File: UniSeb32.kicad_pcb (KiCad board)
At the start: 4 copper layers, 72 x 100 mm, 60 parts, among them J1 IO, J101 Micro_SD_Card_Det, J2 ARJM11C7-114-BA-EW2, J3 Conn_02x05_Odd_Even, J6 SDS011, J7 Conn_01x02_Female, J8 Conn_01x02_Female, U1 mini_esp32, U2 LAN8720A, U3 AMS1117-3.3, U4 AMS5915, U5 module_bme280, U6 RT9400, U7 MCP23008-xSS, U8 HLK-PM01, X1 233-508, X2 233-503, X3 233-504

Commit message: .
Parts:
- removed C5, C6, C7, C8: 10p, Capacitor_SMD:C_0603_1608Metric
- added D101: ESD3.3V88D-LA, Diode_SMD:D_SOD-923, B.Cu at (167.1, 66.9)
- added D102: ESD3.3V88D-LA, Diode_SMD:D_SOD-923, B.Cu at (165.0, 67.1)
- added D103: ESD3.3V88D-LA, Diode_SMD:D_SOD-923, B.Cu at (161.7, 67.1)
- added D104: ESD3.3V88D-LA, Diode_SMD:D_SOD-923, B.Cu at (159.3, 67.1)
- added R101: 10k, Resistor_SMD:R_0603_1608Metric, B.Cu at (159.5, 58.7)
- C3: value 22µ -> 22u
- L1: value L -> FB0805/600R/2A
- moved R12 0.61 mm to (159.9, 62.0), turned to 0 degrees
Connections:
- J2 pad 11: 3V3-2 -> Net-(J2-RLED+)
- J2 pad 12: Net-(J2-Pad12) -> Net-(J2-RLED-)
- R12 pad 1: Net-(J2-Pad12) -> Net-(J2-RLED+)
- R12 pad 2: GND -> 3V3-2
- U2 pad 2: unconnected-(U2-Pad2) -> Net-(J2-RLED-)
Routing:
- net Net-(J2-RLED-): track 0.00 -> 66.1 mm, vias 0 -> 2
- net Net-(J2-Pad12): track 6.44 -> 0.00 mm
- net Net-(J2-RLED+): track 0.00 -> 3.95 mm
- net GND: track 0.00 -> 3.39 mm
- net /TX_P: track 59.7 -> 60.7 mm
- net /RX_N: track 46.5 -> 47.3 mm
- net /RX_P: track 45.4 -> 46.2 mm
- net /TX_N: track 60.1 -> 60.8 mm
- net 3V3-2: track 80.8 -> 81.0 mm, vias 9 -> 10

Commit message: .
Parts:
- removed JP3: SolderJumper_2_Open, Jumper:SolderJumper-2_P1.3mm_Open_Pad1.0x1.5mm
- added C5: 100n, Capacitor_SMD:C_0603_1608Metric, B.Cu at (158.8, 90.5)
- C14, C15: footprint Capacitor_SMD:C_0603_1608Metric -> Capacitor_SMD:C_1206_3216Metric
- moved C15 2.55 mm to (171.5, 61.8)
- moved C14 2.51 mm to (152.8, 61.8)
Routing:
- net /SCL: track 121.3 -> 123.6 mm
- net Net-(C15-Pad1): track 2.62 -> 4.62 mm
- net Net-(C14-Pad1): track 2.62 -> 4.52 mm
- net 3V3-2: track 81.0 -> 82.7 mm
- net /SDA: track 117.4 -> 118.1 mm
- net +5V: track 234.8 -> 235.4 mm

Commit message: finished routing
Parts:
- removed C11: 10n, Capacitor_SMD:C_0603_1608Metric
- removed C14, C15: 1n, Capacitor_SMD:C_1206_3216Metric
- removed C3: 22u, Capacitor_SMD:C_1206_3216Metric
- removed C9: 10u, Capacitor_SMD:C_0603_1608Metric
- removed D102, D103, D104: ESD3.3V88D-LA, Diode_SMD:D_SOD-923
- removed R14: 12.1k, Resistor_SMD:R_0603_1608Metric
- removed R16, R19, R20: 10k, Resistor_SMD:R_0603_1608Metric
- removed U2: LAN8720A, Package_DFN_QFN:QFN-24-1EP_4x4mm_P0.5mm_EP2.6x2.6mm
- added C101: 100n, Capacitor_SMD:C_0603_1608Metric, B.Cu at (165.8, 91.0)
- added C102: 47µ, Capacitor_SMD:C_0805_2012Metric, B.Cu at (148.2, 107.8)
- added C103: 47µ, Capacitor_SMD:C_0805_2012Metric, B.Cu at (151.0, 107.8)
- added C104: 100n, Capacitor_SMD:C_0603_1608Metric, B.Cu at (162.0, 105.5)
- added C16: 100n, Capacitor_SMD:C_0603_1608Metric, B.Cu at (157.5, 91.0)
- added R102: 10k, Resistor_SMD:R_0603_1608Metric, B.Cu at (166.0, 58.8)
- added U101: RTL8201F-VB-CG, UniSeb32:QFN_8201F-VB-CG_RTK, B.Cu at (163.8, 98.0)
- C12: value 2.2µ -> 47µ; footprint Capacitor_SMD:C_0603_1608Metric -> Capacitor_SMD:C_0805_2012Metric
- D101: value ESD3.3V88D-LA -> SM712_SOT23; footprint Diode_SMD:D_SOD-923 -> Package_TO_SOT_SMD:SOT-23
- R15: value 10k -> 2.49k 1%
- moved D101 43.2 mm to (154.5, 108.2), turned to -90 degrees
- moved C5 23.7 mm to (173.5, 72.0), turned to 180 degrees
- moved C4 21.4 mm to (159.8, 91.0), turned to -90 degrees
- moved C12 15.6 mm to (158.5, 106.5)
- moved R18 14.9 mm to (161.8, 91.0), turned to 90 degrees
- moved C13 14.2 mm to (158.2, 102.8), turned to -90 degrees
- moved R15 11.8 mm to (160.2, 102.8), turned to 90 degrees
- moved C10 4.67 mm to (164.8, 103.8)
- moved R17 4.27 mm to (169.8, 100.0)
- moved R10 3.25 mm to (155.5, 98.0), turned to -90 degrees
- moved R11 3.25 mm to (157.5, 97.5), turned to 90 degrees
- moved R13 3.25 mm to (157.5, 94.2), turned to -90 degrees
- moved R9 3.25 mm to (155.5, 101.2), turned to 90 degrees
- moved L1 1.00 mm to (153.5, 104.8), turned to 0 degrees
- moved R8 0.67 mm to (164.5, 62.0), turned to 180 degrees
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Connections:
- C10 pad 1: 3V3-2 -> Net-(U101-DVDD10OUT)
- C12 pad 1: Net-(U2-VDDCR) -> +3.3VA
- C13 pad 1: +3.3V -> Net-(U101-AVDD10OUT)
- C4 pad 2: 3V3-2 -> +3.3VA
- C5 pad 2: 3V3-2 -> Net-(J2-RCT)
- D101 pad 1: /TX_P -> +3.3V
- D101 pad 2: GND -> +3.3VA
- J2 pad 12: Net-(J2-RLED-) -> GND
- J2 pad 14: Net-(J2-LLED-) -> GND
- J2 pad 4: 3V3-2 -> Net-(J2-RCT)
- J2 pad 9: 3V3-2 -> Net-(J2-RCT)
- J2 pad SH1: Net-(C15-Pad1) -> GND
- J2 pad SH2: Net-(C14-Pad1) -> GND
- L1 pad 2: 3V3-2 -> +3.3VA
- R10 pad 1: 3V3-2 -> Net-(C16-Pad1)
- R101 pad 2: Net-(J2-RLED-) -> Net-(U101-LED1/PHYAD[1])
- R11 pad 1: 3V3-2 -> Net-(C16-Pad1)
- R12 pad 1: Net-(J2-RLED+) -> Net-(U101-LED1/PHYAD[1])
- R12 pad 2: 3V3-2 -> Net-(J2-RLED+)
- R13 pad 1: 3V3-2 -> Net-(C16-Pad1)
- R17 pad 2: 3V3-2 -> +3.3V
- R18 pad 1: /EMAC_CRS_DV -> Net-(U101-RXDV)
- R18 pad 2: 3V3-2 -> +3.3V
- R8 pad 1: Net-(J2-LLED-) -> Net-(J2-LLED+)
- R8 pad 2: GND -> Net-(U101-LED0/PHYAD[0]/PMEB)
- R9 pad 1: 3V3-2 -> Net-(C16-Pad1)
- U1 pad 2: unconnected-(U1-RST-Pad2) -> /RST
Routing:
- net 3V3-2: track 82.7 -> 0.00 mm, vias 10 -> 0
- net Net-(U101-LED1/PHYAD[1]): track 0.00 -> 71.9 mm, vias 0 -> 4
- net Net-(J2-RLED-): track 65.9 -> 0.00 mm, vias 2 -> 0
- net Net-(U101-LED0/PHYAD[0]/PMEB): track 0.00 -> 61.9 mm, vias 0 -> 2
- net +3.3VA: track 0.00 -> 41.4 mm, vias 0 -> 2
- net Net-(J2-LLED+): track 44.7 -> 3.57 mm, vias 1 -> 0
- net /RST: track 0.00 -> 27.3 mm, vias 0 -> 1
- net Net-(J2-RCT): track 0.00 -> 19.1 mm, vias 0 -> 1
- net Net-(C16-Pad1): track 0.00 -> 18.0 mm, vias 0 -> 3
- net /IO5_RST: track 17.8 -> 0.00 mm
- net /IO17_RCLK: track 11.4 -> 26.8 mm, vias 0 -> 1
- net +3.3V: track 188.8 -> 176.4 mm, vias 6 -> 9
- net GND: track 3.39 -> 10.7 mm, vias 20 -> 26
- net /EMAC_RXD1: track 28.2 -> 20.8 mm
- net /RX_N: track 47.3 -> 40.0 mm
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- added copper zone on In2.Cu, net +3.3V
- removed copper zone on In2.Cu, net 3V3-2

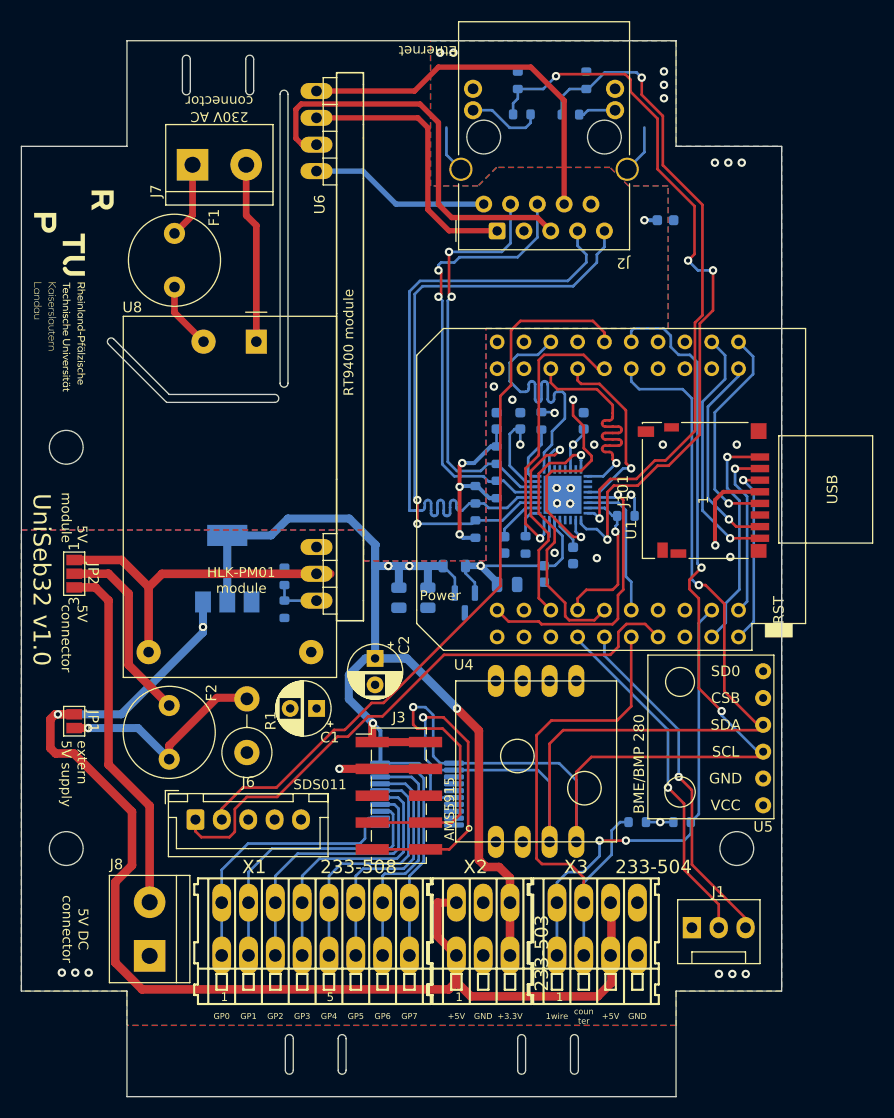
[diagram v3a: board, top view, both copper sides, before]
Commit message: removed SJ1, rename SJ2 -> SJ1, added SJ2 to change pin2 usage of J1
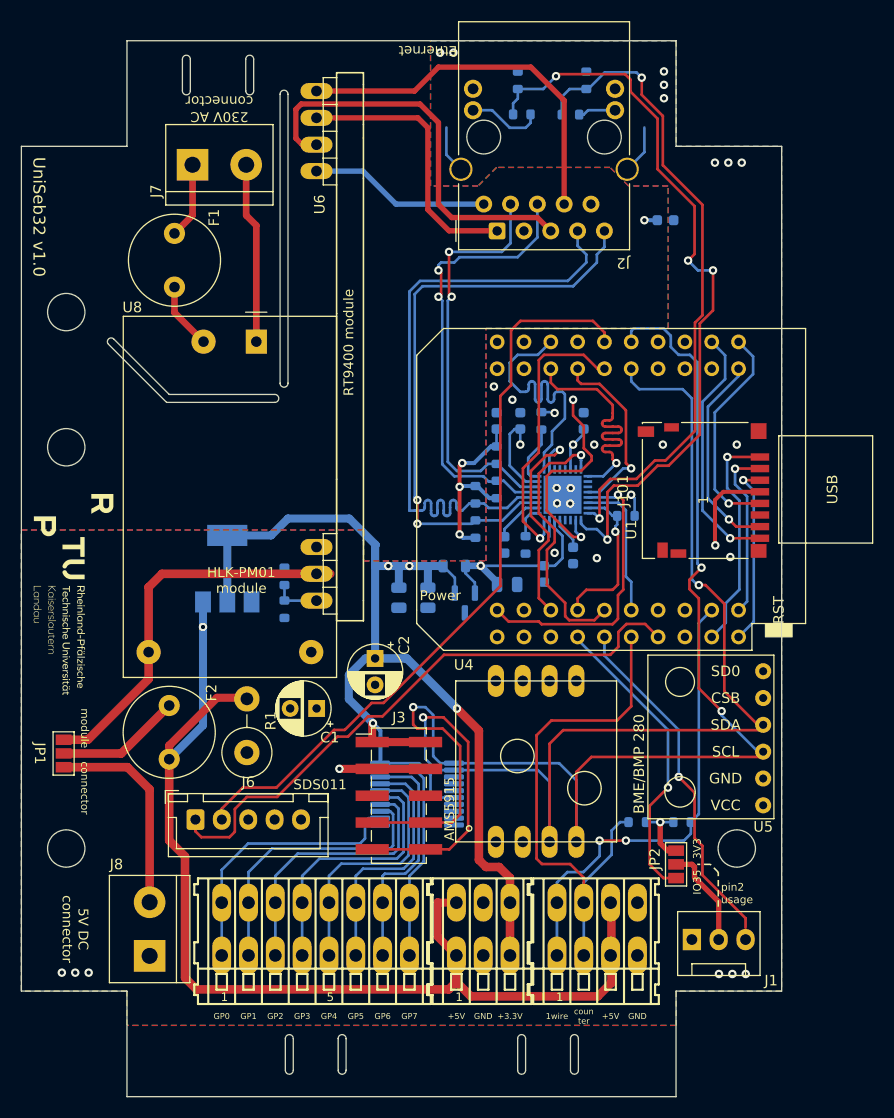
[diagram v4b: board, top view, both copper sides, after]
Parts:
- removed H1, H2, H3: MountingHole, MountingHole:MountingHole_3.2mm_M3
- JP1: value SolderJumper_2_Open -> SolderJumper_3_Open; footprint Jumper:SolderJumper-2_P1.3mm_Open_Pad1.0x1.5mm -> Jumper:SolderJumper-3_P1.3mm_Open_Pad1.0x1.5mm_NumberLabels
- moved JP2 63.3 mm to (174.5, 133.0)
- moved JP1 3.22 mm to (116.5, 122.5)
- moved J1 1.12 mm to (176.0, 140.1)
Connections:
- F2 pad 1: Net-(JP2-C) -> Net-(JP1-C)
- F2 pad 2: VCC -> +5V
- J1 pad 2: /IO35 -> Net-(J1-Pin_2)
- JP1 pad 1: +5V -> Net-(JP1-A)
- JP1 pad 2: VCC -> Net-(JP1-C)
- JP2 pad 1: Net-(JP2-A) -> +3.3V
- JP2 pad 2: Net-(JP2-C) -> Net-(J1-Pin_2)
- JP2 pad 3: Net-(J8-Pin_2) -> /IO35
- R1 pad 2: VCC -> +5V
- R7 pad 2: Net-(JP2-A) -> Net-(JP1-A)
- U6 pad P$6: Net-(JP2-A) -> Net-(JP1-A)
- U8 pad 4: Net-(JP2-A) -> Net-(JP1-A)
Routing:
- net Net-(JP1-A): track 0.00 -> 40.2 mm
- net Net-(JP2-A): track 35.3 -> 0.00 mm
- net VCC: track 20.9 -> 0.00 mm, vias 1 -> 0
- net Net-(JP2-C): track 18.1 -> 0.00 mm
- net Net-(J8-Pin_2): track 34.0 -> 19.7 mm
- net Net-(JP1-C): track 0.00 -> 11.9 mm
- net Net-(J1-Pin_2): track 0.00 -> 9.68 mm
- net +5V: track 235.4 -> 226.2 mm, vias 3 -> 2
- net /IO35: track 33.1 -> 28.8 mm
- net +3.3V: track 176.4 -> 180.2 mm
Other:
- outline, holes or cut-outs redrawn
- board text added: "3V3"
- board text added: "IO35"
- board text added: "connector"
- board text added: "module"
- board text added: "pin2 usage"
- board text removed: "5V connector"
- board text removed: "5V module"
- board text removed: "extern 5V supply"

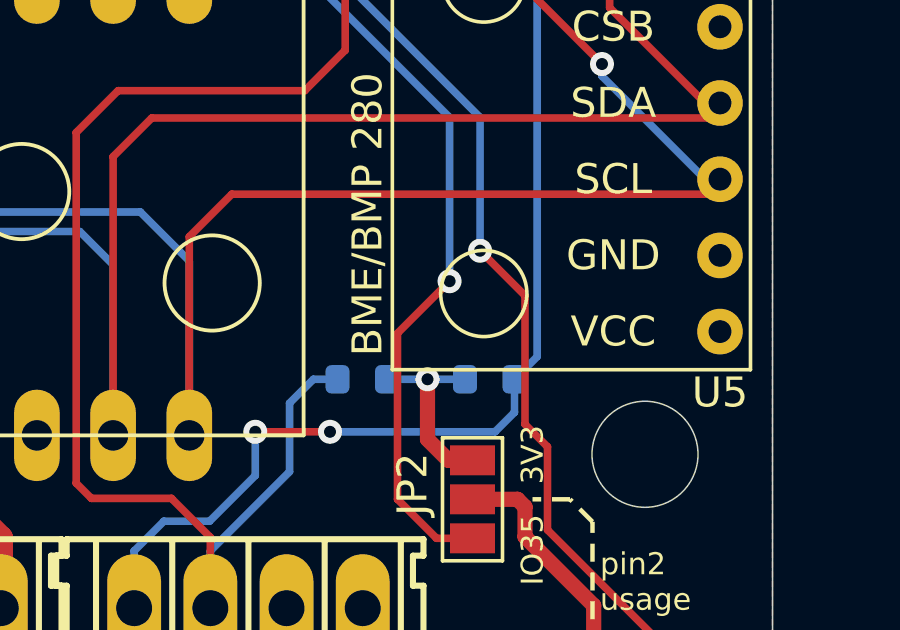
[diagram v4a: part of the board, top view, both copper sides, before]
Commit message: added pullup for pin3 of J1
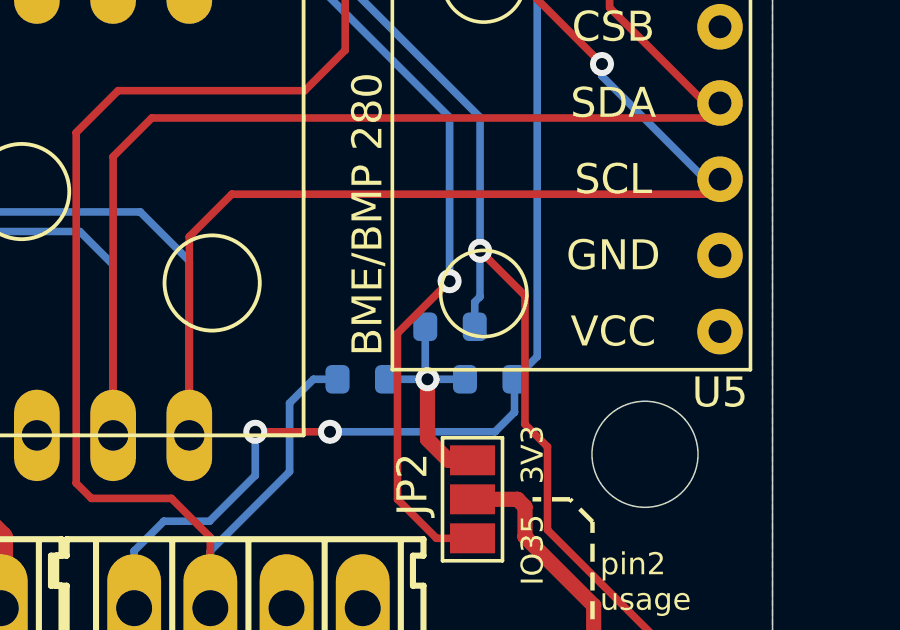
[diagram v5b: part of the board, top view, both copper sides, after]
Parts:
- added R2: 4,7k, Resistor_SMD:R_0603_1608Metric, B.Cu at (173.8, 127.2)
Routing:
- net /IO33: track 33.1 -> 35.9 mm
- net +3.3V: track 180.2 -> 182.0 mm
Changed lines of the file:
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@@
         (effects (font (size 1 1) (thickness 0.15)))
     )
-    (fp_text value "Conn_02x05_Odd_Even" (at 0 7.41) (layer "F.Fab")
+    (fp_text value "Conn_02x05_Odd_Even" (at 0 7.41) (layer "F.Fab") hide
         (effects (font (size 1 1) (thickness 0.15)))
     )
@@
     )
   )
+  (footprint "Resistor_SMD:R_0603_1608Metric" (layer "B.Cu")
+    (at 173.75 127.25 180)
+    (descr "Resistor SMD 0603 (1608 Metric), square (rectangular) end terminal, IPC_7351 nominal, (Body size source: IPC-SM-782 page 72, https://www.pcb-3d.com/wordpress/wp-content/uploads/ipc-sm-782a_amendment_1_and_2.pdf), generated with kicad-footprint-generator")
+    (tags "resistor")
+    (property "JLC" "0603")
+    (property "LCSC" "C23162")
+    (property "Sheetfile" "UniSeb32.kicad_sch")
+    (property "Sheetname" "")
+    (property "ki_description" "Resistor")
+    (property "ki_keywords" "R res resistor")
+    (attr smd)
+    (fp_text reference "R2" (at 0 1.43) (layer "B.SilkS")
+        (effects (font (size 1 1) (thickness 0.15)) (justify mirror))
+    )
+    (fp_text value "4,7k" (at 0 -1.43) (layer "B.Fab")
+        (effects (font (size 1 1) (thickness 0.15)) (justify mirror))
+    )
+    (fp_text user "${REFERENCE}" (at 0 0) (layer "B.Fab")
+        (effects (font (size 0.4 0.4) (thickness 0.06)) (justify mirror))
+    )
+    (fp_line (start -0.237258 -0.5225) (end 0.237258 -0.5225)
+      (stroke (width 0.12) (type solid)) (layer "B.SilkS"))
+    (fp_line (start -0.237258 0.5225) (end 0.237258 0.5225)
+      (stroke (width 0.12) (type solid)) (layer "B.SilkS"))
+    (fp_line (start -1.48 -0.73) (end -1.48 0.73)
+      (stroke (width 0.05) (type solid)) (layer "B.CrtYd"))
+    (fp_line (start -1.48 0.73) (end 1.48 0.73)
+      (stroke (width 0.05) (type solid)) (layer "B.CrtYd"))
+    (fp_line (start 1.48 -0.73) (end -1.48 -0.73)
+      (stroke (width 0.05) (type solid)) (layer "B.CrtYd"))
+    (fp_line (start 1.48 0.73) (end 1.48 -0.73)
+      (stroke (width 0.05) (type solid)) (layer "B.CrtYd"))
+    (fp_line (start -0.8 -0.4125) (end -0.8 0.4125)
+      (stroke (width 0.1) (type solid)) (layer "B.Fab"))
+    (fp_line (start -0.8 0.4125) (end 0.8 0.4125)
+      (stroke (width 0.1) (type solid)) (layer "B.Fab"))
+    (fp_line (start 0.8 -0.4125) (end -0.8 -0.4125)
+      (stroke (width 0.1) (type solid)) (layer "B.Fab"))
+    (fp_line (start 0.8 0.4125) (end 0.8 -0.4125)
+      (stroke (width 0.1) (type solid)) (layer "B.Fab"))
+    (pad "1" smd roundrect (at -0.825 0 180) (size 0.8 0.95) (layers "B.Cu" "B.Paste" "B.Mask") (roundrect_rratio 0.25)
+      (net 8 "/IO33") (pintype "passive"))
+    (pad "2" smd roundrect (at 0.825 0 180) (size 0.8 0.95) (layers "B.Cu" "B.Paste" "B.Mask") (roundrect_rratio 0.25)
+      (net 3 "+3.3V") (pintype "passive"))
+    (model "${KICAD6_3DMODEL_DIR}/Resistor_SMD.3dshapes/R_0603_1608Metric.wrl"
+      (offset (xyz 0 0 0))
+      (scale (xyz 1 1 1))
+      (rotate (xyz 0 0 0))
+    )
+  )
   (footprint "Capacitor_SMD:C_0603_1608Metric" (layer "B.Cu")
     (at 159.75 91 -90)
@@
   (segment (start 147.25 104.75) (end 146 104.75) (width 0.762) (layer "B.Cu") (net 3))
   (segment (start 161.75 90.175) (end 162.925 90.175) (width 0.254) (layer "B.Cu") (net 3))
+  (segment (start 172.925 128.925) (end 173 129) (width 0.254) (layer "B.Cu") (net 3))
   (segment (start 151 104.75) (end 151 106.8) (width 0.762) (layer "B.Cu") (net 3))
   (segment (start 146.5 120.338) (end 146.5 123.3897) (width 0.381) (layer "B.Cu") (net 3))
@@
   (segment (start 164.75 93.25) (end 164.500189 93.499811) (width 0.254) (layer "B.Cu") (net 3))
   (segment (start 143.557 100.25) (end 146.05 102.743) (width 0.762) (layer "B.Cu") (net 3))
+  (segment (start 172.925 127.25) (end 172.925 128.925) (width 0.254) (layer "B.Cu") (net 3))
   (segment (start 151.25 126.25) (end 151.6736 126.6736) (width 0.254) (layer "B.Cu") (net 3))
   (segment (start 165.75 92.25) (end 165.75 91.775) (width 0.254) (layer "B.Cu") (net 3))
@@
   (segment (start 174.752 120.269) (end 167.717 113.234) (width 0.254) (layer "B.Cu") (net 8))
   (segment (start 174.752 124.714) (end 174.752 120.269) (width 0.254) (layer "B.Cu") (net 8))
+  (segment (start 174.75 126.25) (end 174.75 124.716) (width 0.254) (layer "B.Cu") (net 8))
   (segment (start 167.717 113.234) (end 167.717 111.464) (width 0.254) (layer "B.Cu") (net 8))
+  (segment (start 174.575 126.425) (end 174.75 126.25) (width 0.254) (layer "B.Cu") (net 8))
+  (segment (start 174.575 124.891) (end 174.752 124.714) (width 0.254) (layer "B.Cu") (net 8))
+  (segment (start 174.575 127.25) (end 174.575 126.425) (width 0.254) (layer "B.Cu") (net 8))
+  (segment (start 174.75 124.716) (end 174.752 124.714) (width 0.254) (layer "B.Cu") (net 8))
   (segment (start 172 133) (end 172 127.466) (width 0.254) (layer "F.Cu") (net 9))
   (segment (start 174.5 134.3) (end 173.3 134.3) (width 0.254) (layer "F.Cu") (net 9))
